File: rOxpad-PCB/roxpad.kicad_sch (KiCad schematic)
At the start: 4 parts

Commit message: fix pinout (thanks Bexin!)
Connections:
- net at Left_sensor1.1 (VDD), Middle_Sensor1.1 (VDD), Right_Sensor1.1 (VDD): now also Pi_Pico1.36 (3V3_OUT); no longer Pi_Pico1.40 (VBUS)
- net at Middle_Sensor1.2 (OUT): now also Pi_Pico1.32 (GP27); no longer Pi_Pico1.26 (GP20)
- net at Right_Sensor1.2 (OUT): now also Pi_Pico1.31 (GP26); no longer Pi_Pico1.25 (GP19)
- net at Pi_Pico1.27 (GP21): no longer Left_sensor1.2 (OUT)
- net at Pi_Pico1.34 (GP28): now also Left_sensor1.2 (OUT)
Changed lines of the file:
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@@
 (kicad_sch (version 20230121) (generator eeschema)
   (paper "A4")
-  (junction (at 125.095 51.435) (diameter 0) (color 0 0 0 0)
+  (junction (at 125.095 56.515) (diameter 0) (color 0 0 0 0)
   )
   (junction (at 144.78 51.435) (diameter 0) (color 0 0 0 0)
@@
   (junction (at 160.02 131.445) (diameter 0) (color 0 0 0 0)
   )
-  (wire (pts (xy 125.095 51.435) (xy 125.095 92.71))
+  (wire (pts (xy 125.095 51.435) (xy 125.095 56.515))
+    (stroke (width 0) (type default))
+  )
+  (wire (pts (xy 114.935 92.075) (xy 119.38 92.075))
+    (stroke (width 0) (type default))
+  )
+  (wire (pts (xy 114.935 94.615) (xy 121.285 94.615))
     (stroke (width 0) (type default))
   )
   (wire (pts (xy 160.02 131.445) (xy 140.335 131.445))
+    (stroke (width 0) (type default))
+  )
+  (wire (pts (xy 114.935 56.515) (xy 125.095 56.515))
     (stroke (width 0) (type default))
   )
@@
     (stroke (width 0) (type default))
   )
-  (wire (pts (xy 114.935 51.435) (xy 125.095 51.435))
+  (wire (pts (xy 163.195 92.71) (xy 163.195 51.435))
     (stroke (width 0) (type default))
   )
-  (wire (pts (xy 163.195 92.71) (xy 163.195 51.435))
+  (wire (pts (xy 119.38 80.01) (xy 119.38 92.075))
+    (stroke (width 0) (type default))
+  )
+  (wire (pts (xy 114.935 97.155) (xy 123.19 97.155))
     (stroke (width 0) (type default))
   )
@@
     (stroke (width 0) (type default))
   )
-  (wire (pts (xy 119.38 81.915) (xy 114.935 81.915))
-    (stroke (width 0) (type default))
-  )
-  (wire (pts (xy 123.19 86.995) (xy 114.935 86.995))
-    (stroke (width 0) (type default))
-  )
   (wire (pts (xy 170.815 80.01) (xy 170.815 85.09))
     (stroke (width 0) (type default))
@@
     (stroke (width 0) (type default))
   )
-  (wire (pts (xy 119.38 80.01) (xy 119.38 81.915))
-    (stroke (width 0) (type default))
-  )
-  (wire (pts (xy 123.19 85.09) (xy 123.19 86.995))
+  (wire (pts (xy 123.19 85.09) (xy 123.19 97.155))
     (stroke (width 0) (type default))
   )
@@
     (stroke (width 0) (type default))
   )
-  (wire (pts (xy 121.285 82.55) (xy 121.285 84.455))
-    (stroke (width 0) (type default))
-  )
-  (wire (pts (xy 121.285 84.455) (xy 114.935 84.455))
+  (wire (pts (xy 121.285 82.55) (xy 121.285 94.615))
     (stroke (width 0) (type default))
   )
@@
     (stroke (width 0) (type default))
   )
+  (wire (pts (xy 125.095 56.515) (xy 125.095 92.71))
+    (stroke (width 0) (type default))
+  )

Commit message: change ' hall sensor`to proper sensor name
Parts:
- Left_sensor1, Middle_Sensor1, Right_Sensor1: value Hall_Sensor -> SS49E
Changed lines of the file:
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@@
       (effects (font (size 1.27 1.27)))
     )
-    (property "Value" "Hall_Sensor" (at 153.543 94.6912 0)
+    (property "Value" "SS49E" (at 153.543 94.6912 0)
       (effects (font (size 0.9906 0.9906)) (justify right) hide)
     )
@@
       (effects (font (size 1.27 1.27)))
     )
-    (property "Value" "Hall_Sensor" (at 171.958 94.6912 0)
+    (property "Value" "SS49E" (at 171.958 94.6912 0)
       (effects (font (size 0.9906 0.9906)) (justify right) hide)
     )
@@
       (effects (font (size 1.27 1.27)))
     )
-    (property "Value" "Hall_Sensor" (at 133.858 94.6912 0)
+    (property "Value" "SS49E" (at 133.858 94.6912 0)
       (effects (font (size 0.9906 0.9906)) (justify right) hide)
     )

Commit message: changed designations
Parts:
- renumbered Left_sensor1 to H1, Middle_Sensor1 to H2, Right_Sensor1 to H3
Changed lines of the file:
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@@
   (symbol (lib_id "49e:Hall_Sensor") (at 152.4 90.17 90) (unit 1)
     (in_bom yes) (on_board yes) (dnp no) (fields_autoplaced)
-    (property "Reference" "Middle_Sensor1" (at 152.4 95.885 90)
+    (property "Reference" "H2" (at 152.4 96.52 90)
       (effects (font (size 1.27 1.27)))
     )
@@
       (project "roxpad"
         (path "/694accb5-9413-480b-b86e-37ee58c6ddde"
-          (reference "Middle_Sensor1") (unit 1)
+          (reference "H2") (unit 1)
         )
       )
@@
   (symbol (lib_id "49e:Hall_Sensor") (at 170.815 90.17 90) (unit 1)
     (in_bom yes) (on_board yes) (dnp no) (fields_autoplaced)
-    (property "Reference" "Right_Sensor1" (at 170.815 95.885 90)
+    (property "Reference" "H3" (at 170.815 96.52 90)
       (effects (font (size 1.27 1.27)))
     )
@@
       (project "roxpad"
         (path "/694accb5-9413-480b-b86e-37ee58c6ddde"
-          (reference "Right_Sensor1") (unit 1)
+          (reference "H3") (unit 1)
         )
       )
@@
   (symbol (lib_id "49e:Hall_Sensor") (at 132.715 90.17 90) (unit 1)
     (in_bom yes) (on_board yes) (dnp no) (fields_autoplaced)
-    (property "Reference" "Left_sensor1" (at 132.715 96.52 90)
+    (property "Reference" "H1" (at 132.715 96.52 90)
       (effects (font (size 1.27 1.27)))
     )
@@
       (project "roxpad"
         (path "/694accb5-9413-480b-b86e-37ee58c6ddde"
-          (reference "Left_sensor1") (unit 1)
+          (reference "H1") (unit 1)
         )
       )

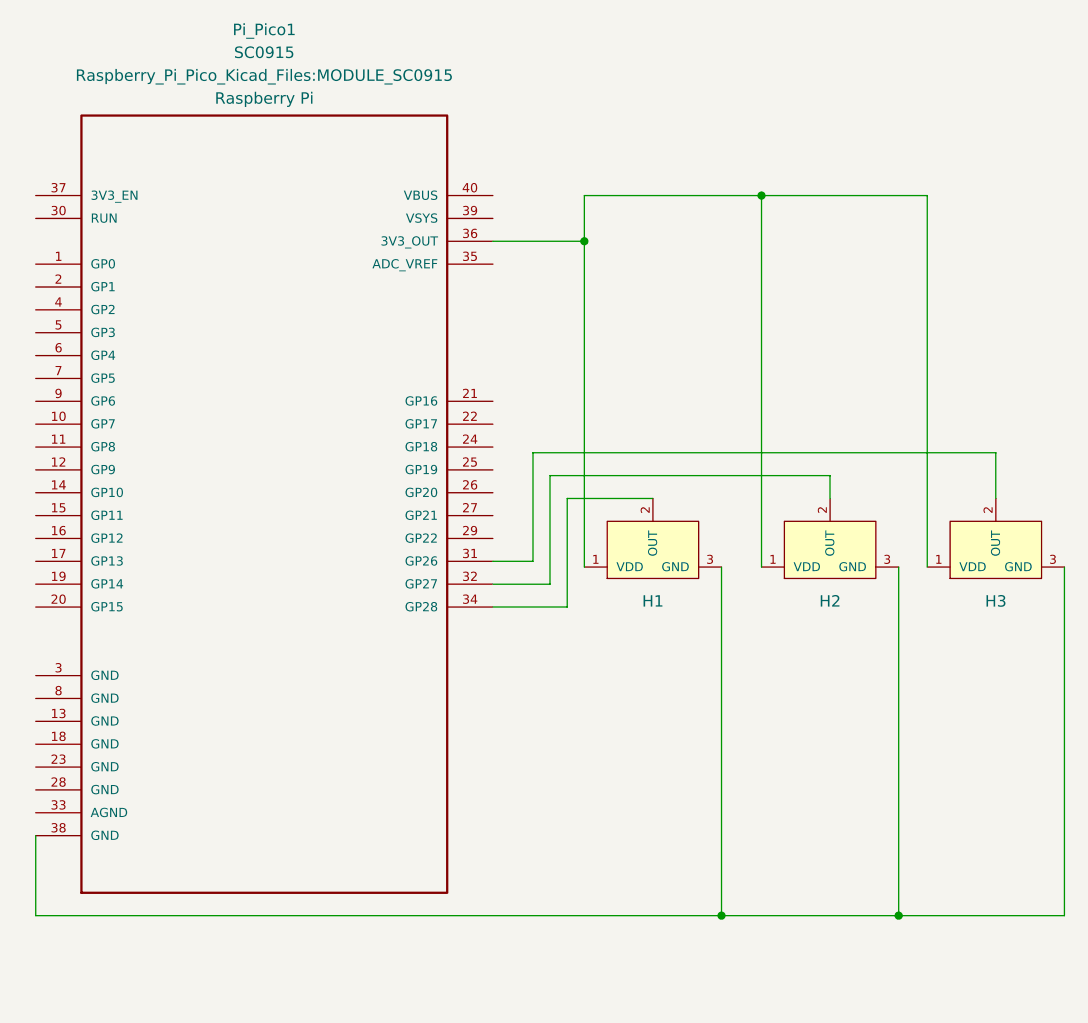
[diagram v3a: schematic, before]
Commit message: changed gnd to agnd
I think this fixes it, won't check
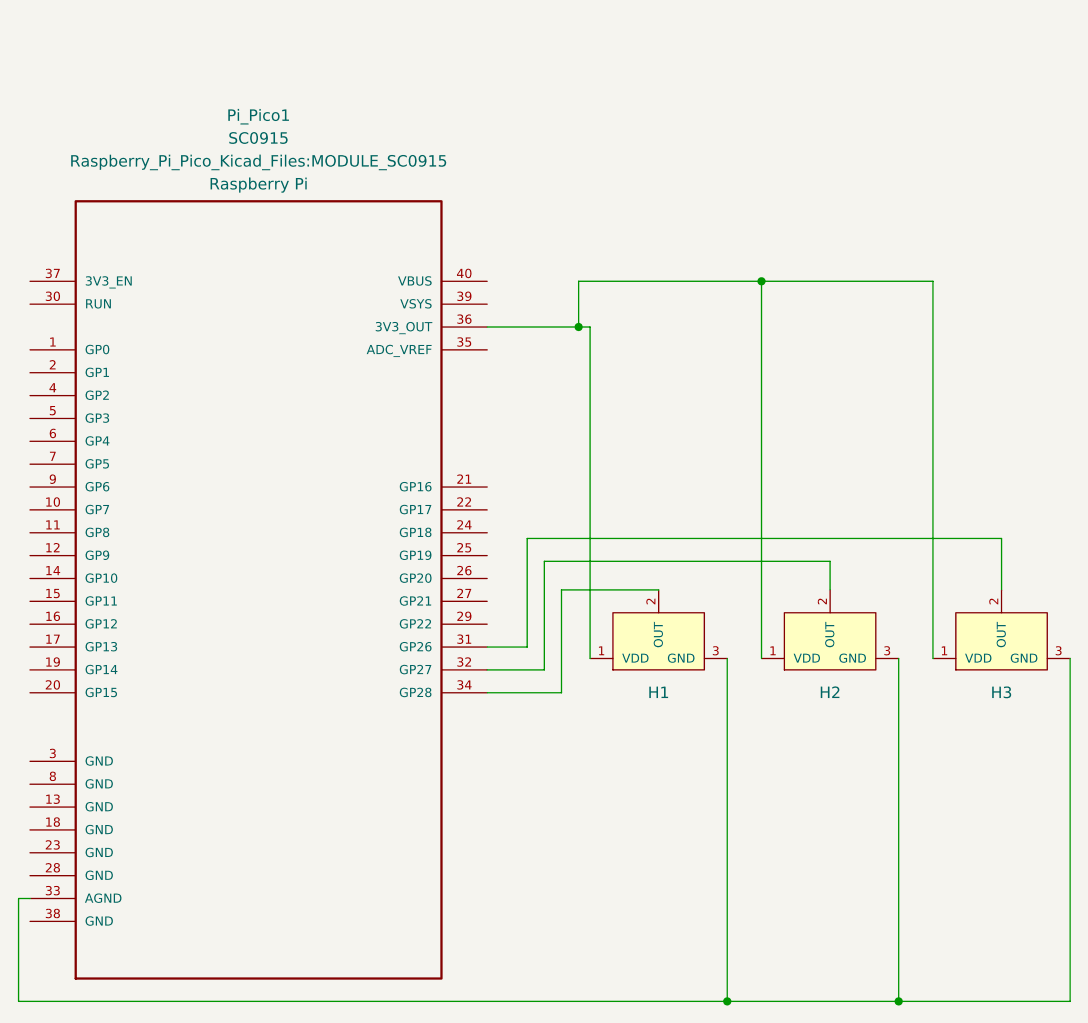
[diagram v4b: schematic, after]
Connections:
- net at H1.3 (GND), H2.3 (GND), H3.3 (GND): now also Pi_Pico1.33 (AGND); no longer Pi_Pico1.38 (GND)
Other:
- moved on the sheet: H1, H2, H3, Pi_Pico1
